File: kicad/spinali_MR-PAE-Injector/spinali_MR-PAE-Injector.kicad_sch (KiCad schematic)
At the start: 0 parts

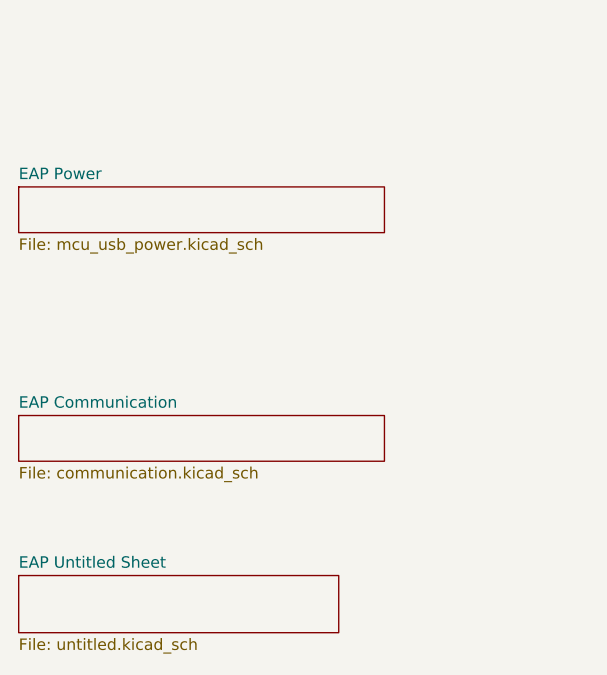
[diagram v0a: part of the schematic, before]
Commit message: Draft design work
Cutting original schematics to basics.
Questions aroung the LM5160 regulator
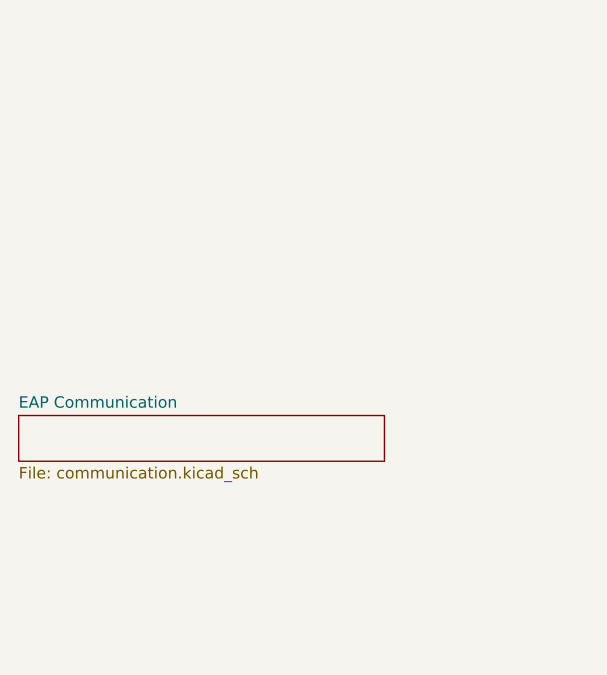
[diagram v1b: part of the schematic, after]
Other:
- removed sheet EAP Power
- removed sheet EAP Untitled Sheet
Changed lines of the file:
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@@
 		(rev "X0")
 		(company "NXP SEMICONDUCTORS B.V.")
-		(comment 1 "Ethernet Adjacent Power Adapter")
-		(comment 3 "DESIGNER: Iain Galloway")
+		(comment 1 "Power Adjacent Ethernet Injector")
+		(comment 3 "DESIGNER: Iain Galloway, Ref:Youri Tils")
 		(comment 4 "CTO SYSTEM INNOVATIONS / MOBILE ROBOTICS DOMAIN")
 	)
@@
 			(font
 				(size 1.27 1.27)
-			)
-		)
-	)
-	(sheet
-		(at 50.8 133.35)
-		(size 35.56 6.35)
-		(exclude_from_sim no)
-		(in_bom yes)
-		(on_board yes)
-		(dnp no)
-		(fields_autoplaced yes)
-		(stroke
-			(width 0.1524)
-			(type solid)
-		)
-		(fill
-			(color 0 0 0 0.0000)
-		)
-		(property "Sheetname" "EAP Untitled Sheet"
-			(at 50.8 132.6384 0)
-			(effects
-				(font
-					(size 1.27 1.27)
-				)
-				(justify left bottom)
-			)
-		)
-		(property "Sheetfile" "untitled.kicad_sch"
-			(at 50.8 140.2846 0)
-			(effects
-				(font
-					(size 1.27 1.27)
-				)
-				(justify left top)
-			)
-		)
-		(instances
-			(project "spinali_MR-T1-EAP-Adapter"
-				(path "/8b469ec1-e800-4d46-8a32-95d77ceae6db"
-					(page "5")
-				)
 			)
 		)
@@
 		)
 		(instances
-			(project "spinali_MR-T1-EAP-Adapter"
+			(project "spinali_MR-PAE-Injector"
 				(path "/8b469ec1-e800-4d46-8a32-95d77ceae6db"
 					(page "7")
-				)
-			)
-		)
-	)
-	(sheet
-		(at 50.8 90.17)
-		(size 40.64 5.08)
-		(exclude_from_sim no)
-		(in_bom yes)
-		(on_board yes)
-		(dnp no)
-		(fields_autoplaced yes)
-		(stroke
-			(width 0.1524)
-			(type solid)
-		)
-		(fill
-			(color 0 0 0 0.0000)
-		)
-		(property "Sheetname" "EAP Power"
-			(at 50.8 89.4584 0)
-			(effects
-				(font
-					(size 1.27 1.27)
-				)
-				(justify left bottom)
-			)
-		)
-		(property "Sheetfile" "mcu_usb_power.kicad_sch"
-			(at 50.8 95.8346 0)
-			(effects
-				(font
-					(size 1.27 1.27)
-				)
-				(justify left top)
-			)
-		)
-		(instances
-			(project "spinali_MR-T1-EAP-Adapter"
-				(path "/8b469ec1-e800-4d46-8a32-95d77ceae6db"
-					(page "5")
 				)
 			)
@@
 		)
 		(instances
-			(project "spinali_MR-T1-EAP-Adapter"
+			(project "spinali_MR-PAE-Injector"
 				(path "/8b469ec1-e800-4d46-8a32-95d77ceae6db"
 					(page "2")

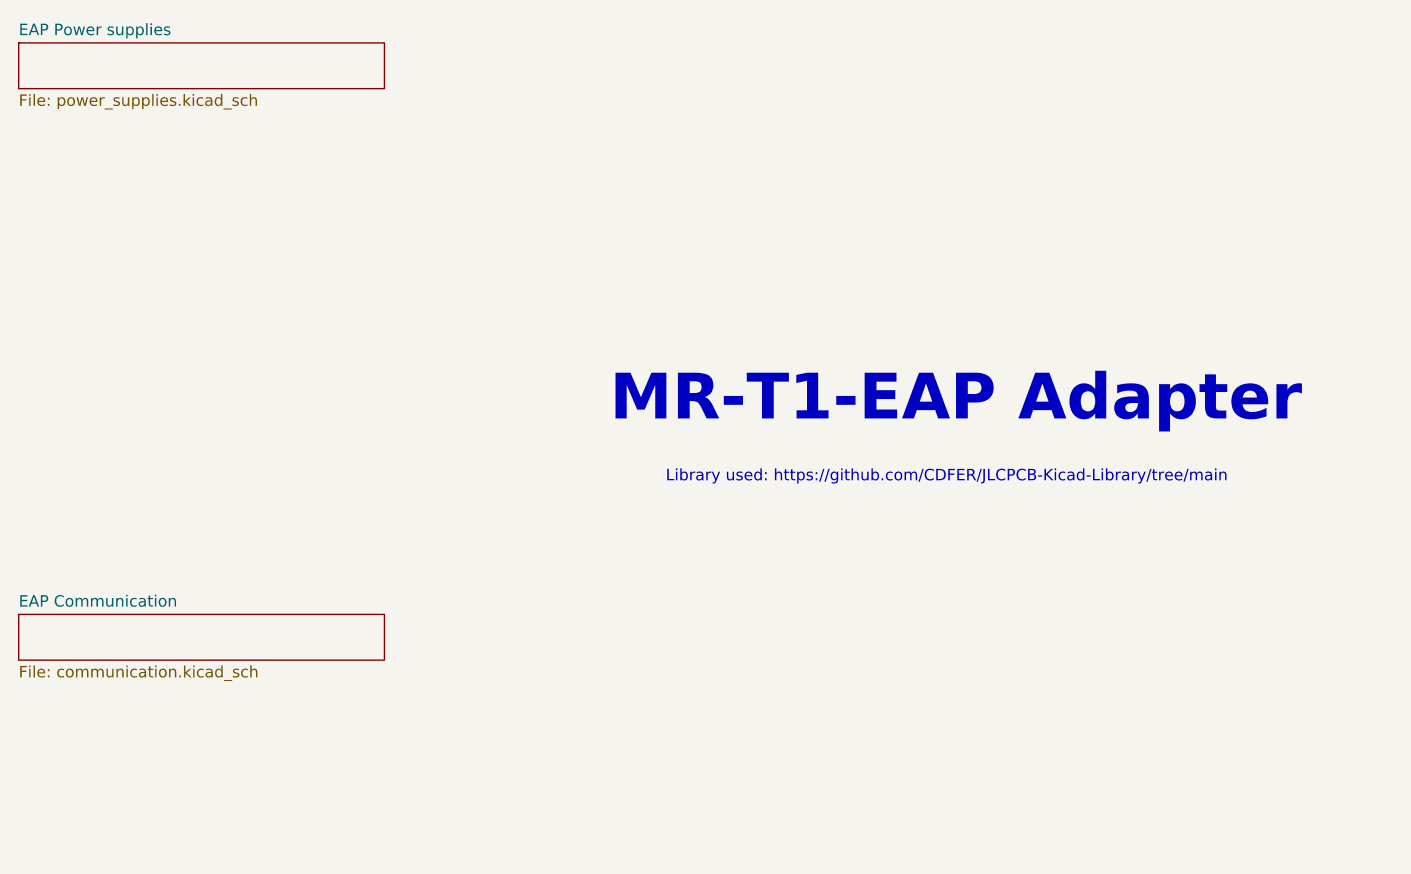
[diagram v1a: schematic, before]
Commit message: ongoing edits and prep
added symbols for 2 pin  and 3 pin headers.
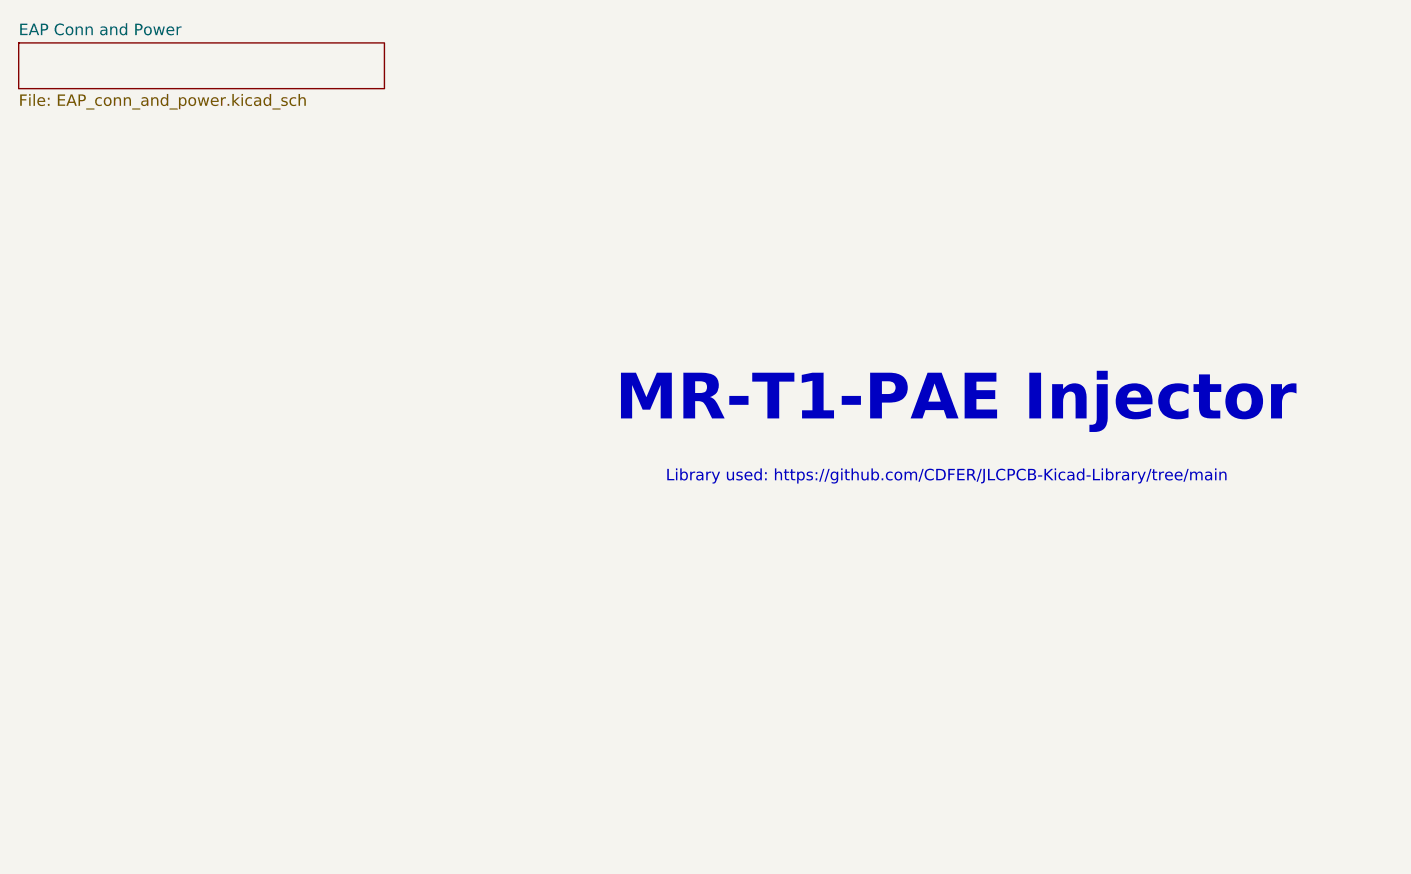
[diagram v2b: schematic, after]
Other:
- sheet EAP Power supplies renamed EAP Conn and Power
- removed sheet EAP Communication
- sheet EAP Conn and Power: file power_supplies.kicad_sch -> EAP_conn_and_power.kicad_sch
- title: MR-T1-EAP Adapter -> MR-T1-PAE Injector
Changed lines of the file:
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@@
 	(paper "A4")
 	(title_block
-		(title "MR-T1-EAP Adapter")
+		(title "MR-T1-PAE Injector")
 		(date "2025-08-28")
 		(rev "X0")
@@
 	)
 	(sheet
-		(at 50.8 115.57)
-		(size 40.64 5.08)
-		(exclude_from_sim no)
-		(in_bom yes)
-		(on_board yes)
-		(dnp no)
-		(fields_autoplaced yes)
-		(stroke
-			(width 0.1524)
-			(type solid)
-		)
-		(fill
-			(color 0 0 0 0.0000)
-		)
-		(property "Sheetname" "EAP Communication"
-			(at 50.8 114.8584 0)
-			(effects
-				(font
-					(size 1.27 1.27)
-				)
-				(justify left bottom)
-			)
-		)
-		(property "Sheetfile" "communication.kicad_sch"
-			(at 50.8 121.2346 0)
-			(effects
-				(font
-					(size 1.27 1.27)
-				)
-				(justify left top)
-			)
-		)
-		(instances
-			(project "spinali_MR-PAE-Injector"
-				(path "/8b469ec1-e800-4d46-8a32-95d77ceae6db"
-					(page "7")
-				)
-			)
-		)
-	)
-	(sheet
 		(at 50.8 52.07)
 		(size 40.64 5.08)
@@
 			(color 0 0 0 0.0000)
 		)
-		(property "Sheetname" "EAP Power supplies"
+		(property "Sheetname" "EAP Conn and Power"
 			(at 50.8 51.3584 0)
 			(effects
@@
 			)
 		)
-		(property "Sheetfile" "power_supplies.kicad_sch"
+		(property "Sheetfile" "EAP_conn_and_power.kicad_sch"
 			(at 50.8 57.7346 0)
 			(effects

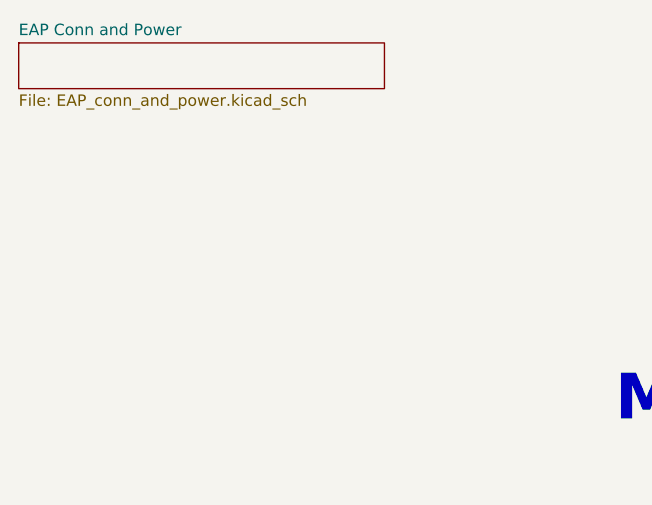
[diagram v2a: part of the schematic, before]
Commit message: Added reverse polarity protection.
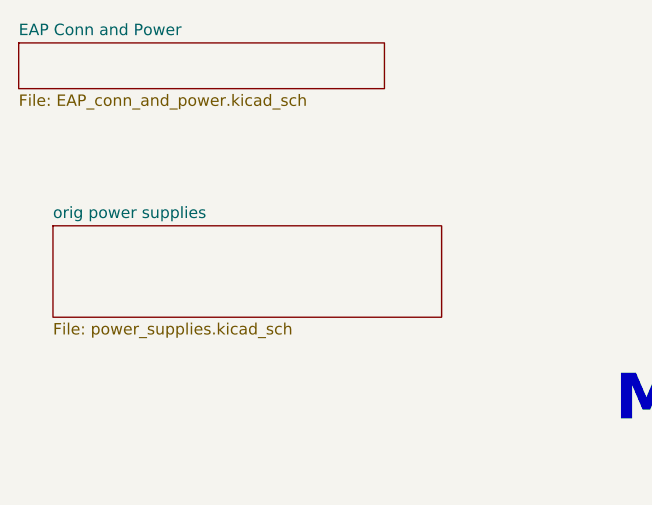
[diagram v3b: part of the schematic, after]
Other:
- added sheet orig power supplies (power_supplies.kicad_sch)
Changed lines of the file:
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@@
+		)
+	)
+	(sheet
+		(at 54.61 72.39)
+		(size 43.18 10.16)
+		(exclude_from_sim no)
+		(in_bom yes)
+		(on_board yes)
+		(dnp no)
+		(fields_autoplaced yes)
+		(stroke
+			(width 0.1524)
+			(type solid)
+		)
+		(fill
+			(color 0 0 0 0.0000)
+		)
+		(property "Sheetname" "orig power supplies"
+			(at 54.61 71.6784 0)
+			(effects
+				(font
+					(size 1.27 1.27)
+				)
+				(justify left bottom)
+			)
+		)
+		(property "Sheetfile" "power_supplies.kicad_sch"
+			(at 54.61 83.1346 0)
+			(effects
+				(font
+					(size 1.27 1.27)
+				)
+				(justify left top)
+			)
+		)
+		(instances
+			(project "spinali_MR-PAE-Injector"
+				(path "/8b469ec1-e800-4d46-8a32-95d77ceae6db"
+					(page "3")
+				)
+			)
 		)
 	)
